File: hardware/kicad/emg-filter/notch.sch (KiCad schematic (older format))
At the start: 9 parts

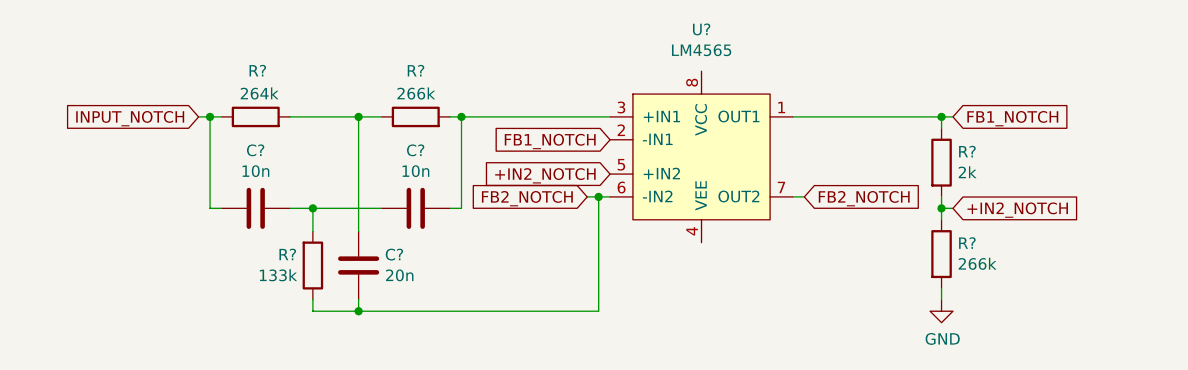
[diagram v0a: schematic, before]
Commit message: added power connections to opamp, renamed input output labels
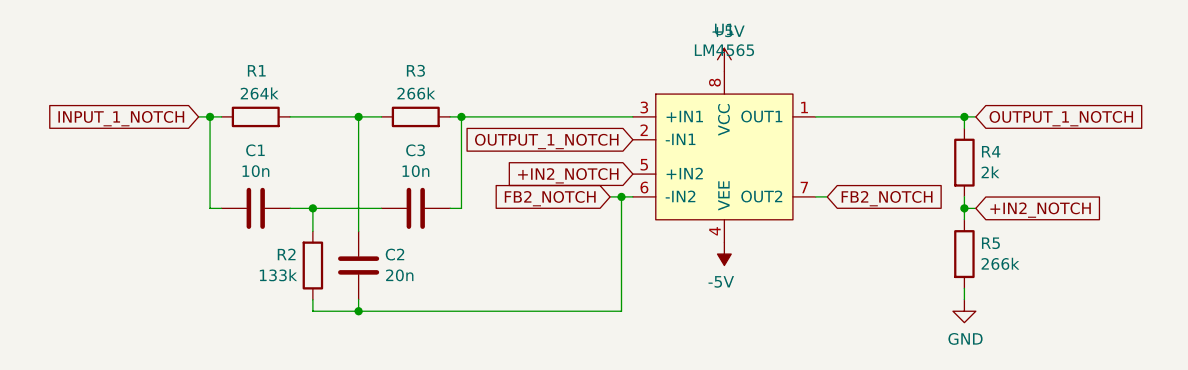
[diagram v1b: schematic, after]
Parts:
- gave numbers to parts that had none: 9
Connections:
- net -5V: now reaches U1.4 (VEE)
- net +5V: now reaches U1.8 (VCC)
- net FB1_NOTCH renamed OUTPUT_1_NOTCH
- net INPUT_NOTCH renamed INPUT_1_NOTCH
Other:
- moved on the sheet: R4, R5, U1
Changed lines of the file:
@@
 $EndDescr
 $Comp
-L emg-filter:LM4565 U?
+L emg-filter:LM4565 U1
 U 1 1 61C3A333
-P 6350 3750
-F 0 "U?" H 6350 4281 50  0000 C CNN
-F 1 "LM4565" H 6350 4190 50  0000 C CNN
-F 2 "" H 7350 3750 50  0001 C CNN
-F 3 "" H 7350 3750 50  0001 C CNN
-	1    6350 3750
-	1    0    0    -1
-$EndComp
-$Comp
-L Device:R R?
+P 6450 3750
+F 0 "U1" H 6450 4281 50  0000 C CNN
+F 1 "LM4565" H 6450 4190 50  0000 C CNN
+F 2 "" H 7450 3750 50  0001 C CNN
+F 3 "" H 7450 3750 50  0001 C CNN
+	1    6450 3750
+	1    0    0    -1
+$EndComp
+$Comp
+L Device:R R1
 U 1 1 61C3B437
 P 4400 3600
-F 0 "R?" V 4600 3550 50  0000 L CNN
+F 0 "R1" V 4600 3550 50  0000 L CNN
 F 1 "264k" V 4500 3500 50  0000 L CNN
 F 2 "" V 4330 3600 50  0001 C CNN
@@
 $EndComp
 $Comp
-L Device:R R?
+L Device:R R3
 U 1 1 61C3B5A9
 P 5100 3600
-F 0 "R?" V 5300 3600 50  0000 C CNN
+F 0 "R3" V 5300 3600 50  0000 C CNN
 F 1 "266k" V 5200 3600 50  0000 C CNN
 F 2 "" V 5030 3600 50  0001 C CNN
@@
 $EndComp
 $Comp
-L Device:R R?
+L Device:R R2
 U 1 1 61C3B840
 P 4650 4250
-F 0 "R?" H 4581 4204 50  0000 R CNN
+F 0 "R2" H 4581 4204 50  0000 R CNN
 F 1 "133k" H 4581 4295 50  0000 R CNN
 F 2 "" V 4580 4250 50  0001 C CNN
@@
 $EndComp
 $Comp
-L Device:C C?
+L Device:C C2
 U 1 1 61C3C1B8
 P 4850 4250
-F 0 "C?" H 4735 4204 50  0000 R CNN
+F 0 "C2" H 4735 4204 50  0000 R CNN
 F 1 "20n" H 4735 4295 50  0000 R CNN
 F 2 "" H 4888 4100 50  0001 C CNN
@@
 $EndComp
 $Comp
-L Device:C C?
+L Device:C C1
 U 1 1 61C3C404
 P 4400 4000
-F 0 "C?" V 4148 4000 50  0000 C CNN
+F 0 "C1" V 4148 4000 50  0000 C CNN
 F 1 "10n" V 4239 4000 50  0000 C CNN
 F 2 "" H 4438 3850 50  0001 C CNN
@@
 $EndComp
 $Comp
-L Device:C C?
+L Device:C C3
 U 1 1 61C3C5ED
 P 5100 4000
-F 0 "C?" V 4848 4000 50  0000 C CNN
+F 0 "C3" V 4848 4000 50  0000 C CNN
 F 1 "10n" V 4939 4000 50  0000 C CNN
 F 2 "" H 5138 3850 50  0001 C CNN
@@
 Wire Wire Line
 	5300 4000 5300 3600
-Text GLabel 5950 3700 0    50   Input ~ 0
-FB1_NOTCH
 Wire Wire Line
 	4650 4400 4650 4450
@@
 Wire Wire Line
 	4850 4450 4850 4400
-Text GLabel 5850 3950 0    50   Input ~ 0
+Text GLabel 5950 3950 0    50   Input ~ 0
 FB2_NOTCH
 Text GLabel 4150 3600 0    50   Input ~ 0
-INPUT_NOTCH
+INPUT_1_NOTCH
 Wire Wire Line
 	4150 3600 4200 3600
 Connection ~ 4200 3600
 Wire Wire Line
-	6750 3950 6800 3950
-Text GLabel 5950 3850 0    50   Input ~ 0
+	6850 3950 6900 3950
+Text GLabel 6050 3850 0    50   Input ~ 0
 +IN2_NOTCH
 Wire Wire Line
-	7400 4000 7400 4050
-Connection ~ 7400 4000
-Wire Wire Line
-	7400 4000 7450 4000
-Text GLabel 7450 4000 2    50   Input ~ 0
+	7500 4000 7500 4050
+Connection ~ 7500 4000
+Wire Wire Line
+	7500 4000 7550 4000
+Text GLabel 7550 4000 2    50   Input ~ 0
 +IN2_NOTCH
 Wire Wire Line
-	7400 4350 7400 4400
-$Comp
-L power:GND #PWR?
+	7500 4350 7500 4400
+$Comp
+L power:GND #PWR0104
 U 1 1 61C7C101
-P 7400 4400
-F 0 "#PWR?" H 7400 4150 50  0001 C CNN
-F 1 "GND" H 7405 4227 50  0000 C CNN
-F 2 "" H 7400 4400 50  0001 C CNN
-F 3 "" H 7400 4400 50  0001 C CNN
-	1    7400 4400
-	1    0    0    -1
-$EndComp
-Connection ~ 7400 3600
-Wire Wire Line
-	6750 3600 7400 3600
-Wire Wire Line
-	7400 3600 7450 3600
-Wire Wire Line
-	7400 3600 7400 3650
-Wire Wire Line
-	7400 3950 7400 4000
-Text GLabel 6800 3950 2    50   Input ~ 0
+P 7500 4400
+F 0 "#PWR0104" H 7500 4150 50  0001 C CNN
+F 1 "GND" H 7505 4227 50  0000 C CNN
+F 2 "" H 7500 4400 50  0001 C CNN
+F 3 "" H 7500 4400 50  0001 C CNN
+	1    7500 4400
+	1    0    0    -1
+$EndComp
+Connection ~ 7500 3600
+Wire Wire Line
+	6850 3600 7500 3600
+Wire Wire Line
+	7500 3600 7550 3600
+Wire Wire Line
+	7500 3600 7500 3650
+Wire Wire Line
+	7500 3950 7500 4000
+Text GLabel 6900 3950 2    50   Input ~ 0
 FB2_NOTCH
-Text GLabel 7450 3600 2    50   Input ~ 0
-FB1_NOTCH
-$Comp
-L Device:R R?
+Text GLabel 7550 3600 2    50   Input ~ 0
+OUTPUT_1_NOTCH
+$Comp
+L Device:R R4
 U 1 1 61C3BC8C
-P 7400 3800
-F 0 "R?" H 7470 3846 50  0000 L CNN
-F 1 "2k" H 7470 3755 50  0000 L CNN
-F 2 "" V 7330 3800 50  0001 C CNN
-F 3 "~" H 7400 3800 50  0001 C CNN
-	1    7400 3800
-	1    0    0    -1
-$EndComp
-$Comp
-L Device:R R?
+P 7500 3800
+F 0 "R4" H 7570 3846 50  0000 L CNN
+F 1 "2k" H 7570 3755 50  0000 L CNN
+F 2 "" V 7430 3800 50  0001 C CNN
+F 3 "~" H 7500 3800 50  0001 C CNN
+	1    7500 3800
+	1    0    0    -1
+$EndComp
+$Comp
+L Device:R R5
 U 1 1 61C3BADF
-P 7400 4200
-F 0 "R?" H 7470 4246 50  0000 L CNN
-F 1 "266k" H 7470 4155 50  0000 L CNN
-F 2 "" V 7330 4200 50  0001 C CNN
-F 3 "~" H 7400 4200 50  0001 C CNN
-	1    7400 4200
-	1    0    0    -1
-$EndComp
-Wire Wire Line
-	5850 3950 5900 3950
-Wire Wire Line
-	5300 3600 5950 3600
+P 7500 4200
+F 0 "R5" H 7570 4246 50  0000 L CNN
+F 1 "266k" H 7570 4155 50  0000 L CNN
+F 2 "" V 7430 4200 50  0001 C CNN
+F 3 "~" H 7500 4200 50  0001 C CNN
+	1    7500 4200
+	1    0    0    -1
+$EndComp
+Wire Wire Line
+	5950 3950 6000 3950
+Wire Wire Line
+	5300 3600 6050 3600
+Wire Wire Line
+	4850 4450 6000 4450
+Wire Wire Line
+	6000 4450 6000 3950
+Connection ~ 6000 3950
+Wire Wire Line
+	6000 3950 6050 3950
+$Comp
+L power:+5V #PWR0105
+U 1 1 61C3E5E0
+P 6450 3400
+F 0 "#PWR0105" H 6450 3250 50  0001 C CNN
+F 1 "+5V" H 6465 3573 50  0000 C CNN
+F 2 "" H 6450 3400 50  0001 C CNN
+F 3 "" H 6450 3400 50  0001 C CNN
+	1    6450 3400
+	1    0    0    -1
+$EndComp
+$Comp
+L power:-5V #PWR0106
+U 1 1 61C3F0F8
+P 6450 4150
+F 0 "#PWR0106" H 6450 4250 50  0001 C CNN
+F 1 "-5V" H 6465 4323 50  0000 C CNN
+F 2 "" H 6450 4150 50  0001 C CNN
+F 3 "" H 6450 4150 50  0001 C CNN
+	1    6450 4150
+	-1   0    0    1
+$EndComp
+Text GLabel 6050 3700 0    50   Input ~ 0
+OUTPUT_1_NOTCH
 Connection ~ 5300 3600
-Wire Wire Line
-	4850 4450 5900 4450
-Wire Wire Line
-	5900 4450 5900 3950
 Connection ~ 4850 4450
-Connection ~ 5900 3950
-Wire Wire Line
-	5900 3950 5950 3950
 $EndSCHEMATC

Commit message: notch x16
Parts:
- added C? (x7): 20n, symbol Device:C
- added C? (x14): 10n, symbol Device:C
- added R? (x14): 266k, symbol Device:R
- added R? (x7): 133k, symbol Device:R
- added R? (x7): 2k, symbol Device:R
- added R? (x7): 264k, symbol Device:R
- added U? (x7): LM4565, symbol emg-filter:LM4565
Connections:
- net +5V: now also U?.8 (VCC), U?.8 (VCC), U?.8 (VCC), U?.8 (VCC), U?.8 (VCC), U?.8 (VCC), U?.8 (VCC)
- net -5V: now also U?.4 (VEE), U?.4 (VEE), U?.4 (VEE), U?.4 (VEE), U?.4 (VEE), U?.4 (VEE), U?.4 (VEE)
- net GND: now also R?.2, R?.2, R?.2, R?.2, R?.2, R?.2, R?.2
- net +IN2_NOTCH renamed +IN2_1_NOTCH
- net FB2_NOTCH: no longer names the net of C2.1, R2.1, U1.6 (-IN2), U1.7 (OUT2)
- new net: C?.1, R?.2, U?.3 (+IN1) (x7)
- new net: C?.1, R?.1, U?.6 (-IN2), U?.7 (OUT2) (x7)
- new net: C?.2, R?.1, R?.2 (x7)
- new net: C?.1, C?.2, R?.2 (x7)
- new net +IN2_2_NOTCH: R?.1, R?.2, U?.5 (+IN2)
- new net +IN2_3_NOTCH: R?.1, R?.2, U?.5 (+IN2)
- new net +IN2_4_NOTCH: R?.1, R?.2, U?.5 (+IN2)
- new net +IN2_5_NOTCH: R?.1, R?.2, U?.5 (+IN2)
- new net +IN2_6_NOTCH: R?.1, R?.2, U?.5 (+IN2)
- new net +IN2_7_NOTCH: R?.1, R?.2, U?.5 (+IN2)
- new net +IN2_8_NOTCH: R?.1, R?.2, U?.5 (+IN2)
- new net INPUT_2_NOTCH: C?.2, R?.1
- new net INPUT_3_NOTCH: C?.2, R?.1
- new net INPUT_4_NOTCH: C?.2, R?.1
- new net INPUT_5_NOTCH: C?.2, R?.1
- new net INPUT_6_NOTCH: C?.2, R?.1
- new net INPUT_7_NOTCH: C?.2, R?.1
- new net INPUT_8_NOTCH: C?.2, R?.1
- new net OUTPUT_2_NOTCH: R?.1, U?.1 (OUT1), U?.2 (-IN1)
- new net OUTPUT_3_NOTCH: R?.1, U?.1 (OUT1), U?.2 (-IN1)
- new net OUTPUT_4_NOTCH: R?.1, U?.1 (OUT1), U?.2 (-IN1)
- new net OUTPUT_5_NOTCH: R?.1, U?.1 (OUT1), U?.2 (-IN1)
- new net OUTPUT_6_NOTCH: R?.1, U?.1 (OUT1), U?.2 (-IN1)
- new net OUTPUT_7_NOTCH: R?.1, U?.1 (OUT1), U?.2 (-IN1)
- new net OUTPUT_8_NOTCH: R?.1, U?.1 (OUT1), U?.2 (-IN1)
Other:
- moved on the sheet: C1, C2, C3, R1, R2, R3, R4, R5, U1

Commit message: annotation
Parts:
- gave numbers to parts that had none: 63
- renumbered C1 to C52, C2 to C56, C3 to C60, R1 to R76, R2 to R80, R3 to R84, R4 to R89, R5 to R90, U1 to U21

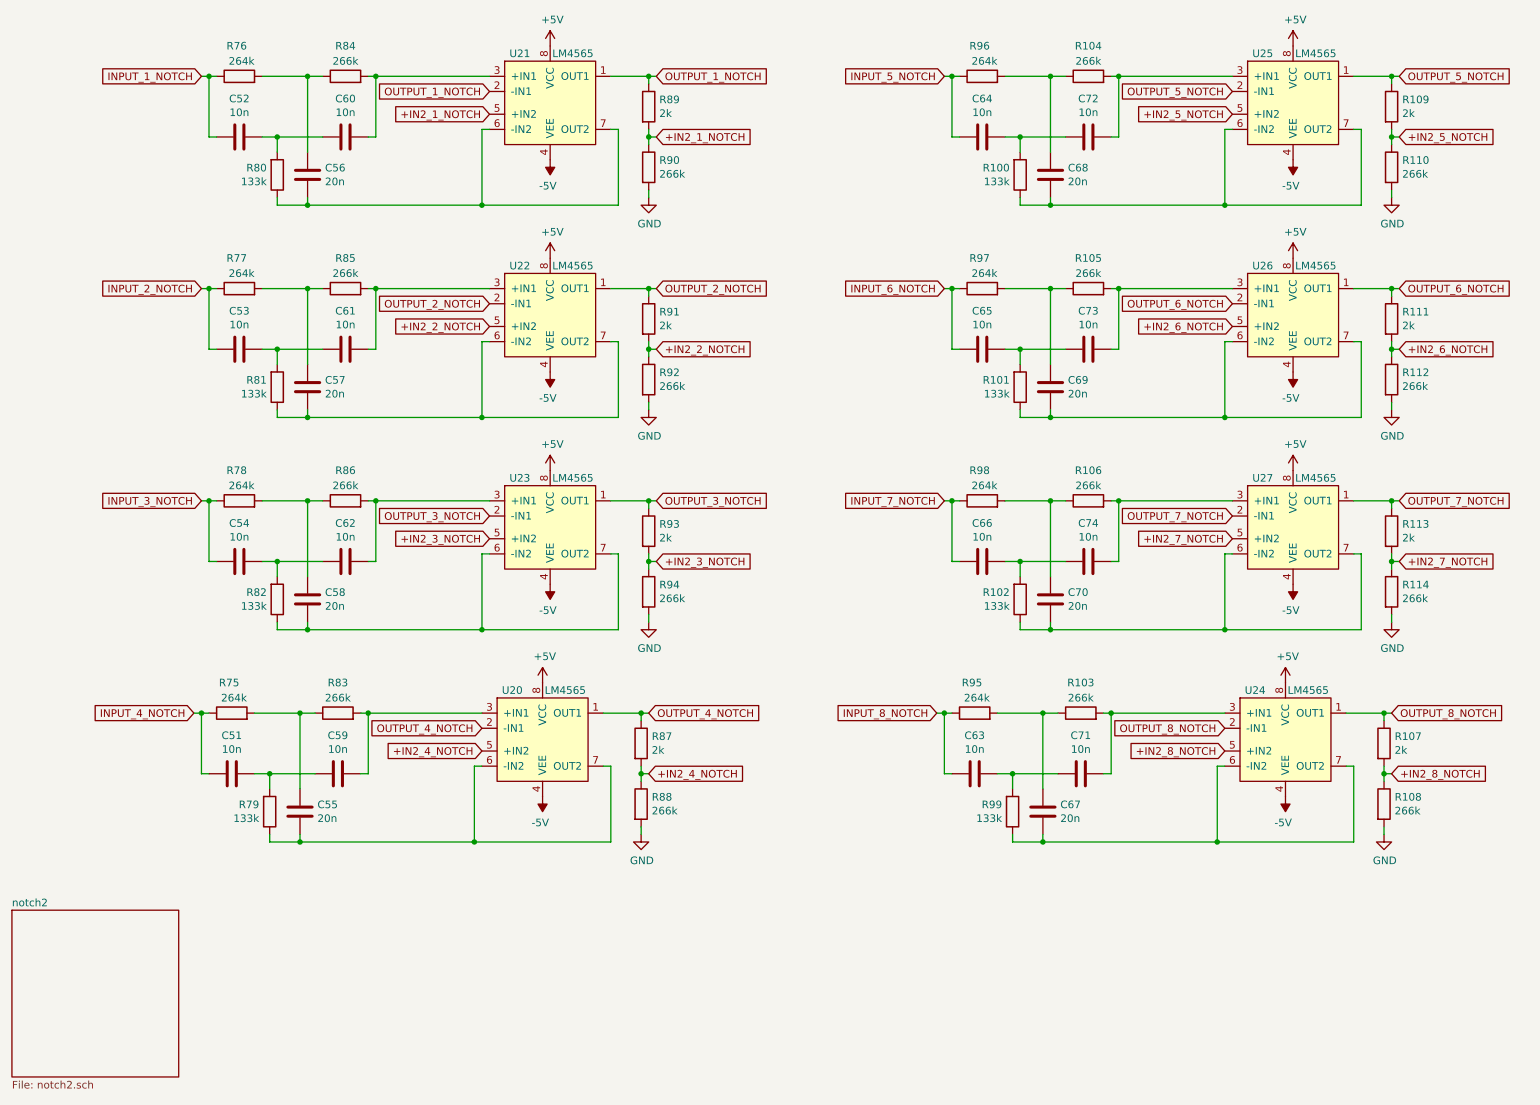
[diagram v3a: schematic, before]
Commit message: linked stages by renaming labels
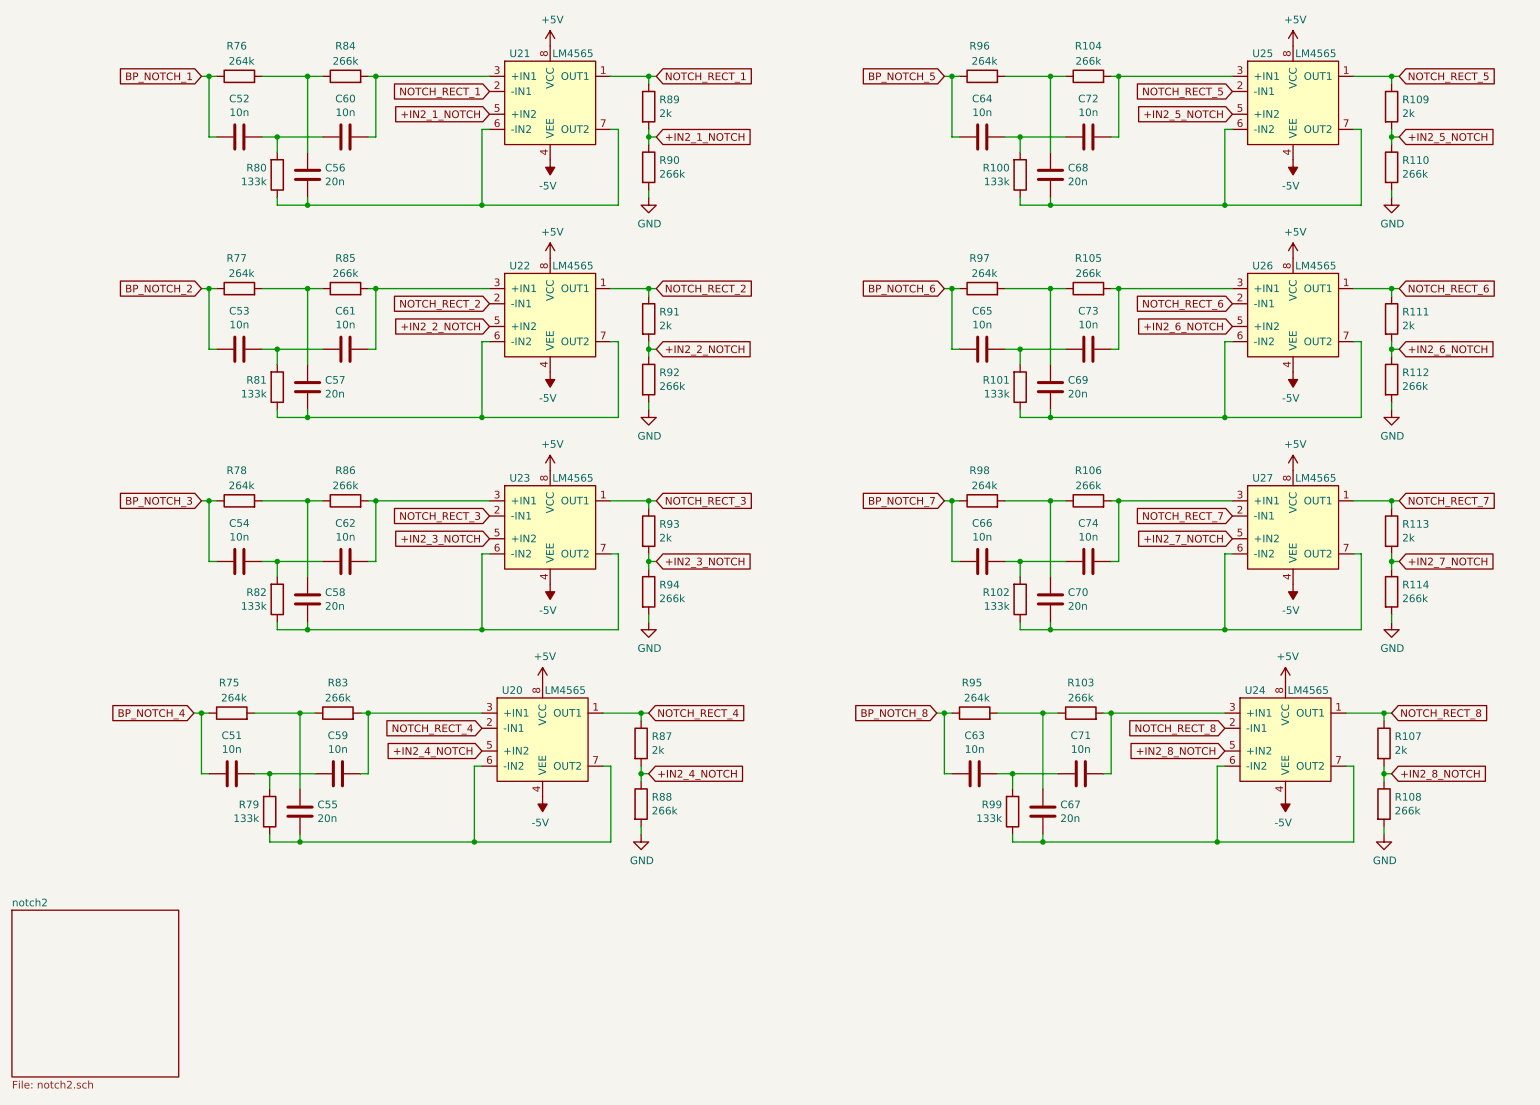
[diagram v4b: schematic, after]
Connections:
- net INPUT_1_NOTCH renamed BP_NOTCH_1
- net INPUT_2_NOTCH renamed BP_NOTCH_2
- net INPUT_3_NOTCH renamed BP_NOTCH_3
- net INPUT_4_NOTCH renamed BP_NOTCH_4
- net INPUT_5_NOTCH renamed BP_NOTCH_5
- net INPUT_6_NOTCH renamed BP_NOTCH_6
- net INPUT_7_NOTCH renamed BP_NOTCH_7
- net INPUT_8_NOTCH renamed BP_NOTCH_8
- net OUTPUT_1_NOTCH renamed NOTCH_RECT_1
- net OUTPUT_2_NOTCH renamed NOTCH_RECT_2
- net OUTPUT_3_NOTCH renamed NOTCH_RECT_3
- net OUTPUT_4_NOTCH renamed NOTCH_RECT_4
- net OUTPUT_5_NOTCH renamed NOTCH_RECT_5
- net OUTPUT_6_NOTCH renamed NOTCH_RECT_6
- net OUTPUT_7_NOTCH renamed NOTCH_RECT_7
- net OUTPUT_8_NOTCH renamed NOTCH_RECT_8
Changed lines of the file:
@@
 Wire Wire Line
 	2600 1850 2600 1800
-Text GLabel 1900 1000 0    50   Input ~ 0
-INPUT_1_NOTCH
 Wire Wire Line
 	1900 1000 1950 1000
@@
 Wire Wire Line
 	4850 1350 4850 1400
-Text GLabel 4900 1000 2    50   Input ~ 0
-OUTPUT_1_NOTCH
 $Comp
 L Device:R R89
@@
 	-1   0    0    1
 $EndComp
-Text GLabel 3800 1100 0    50   Input ~ 0
-OUTPUT_1_NOTCH
 Connection ~ 3050 1000
 Connection ~ 2600 1850
@@
 Wire Wire Line
 	2600 3250 2600 3200
-Text GLabel 1900 2400 0    50   Input ~ 0
-INPUT_2_NOTCH
 Wire Wire Line
 	1900 2400 1950 2400
@@
 Wire Wire Line
 	4850 2750 4850 2800
-Text GLabel 4900 2400 2    50   Input ~ 0
-OUTPUT_2_NOTCH
 $Comp
 L Device:R R91
@@
 	-1   0    0    1
 $EndComp
-Text GLabel 3800 2500 0    50   Input ~ 0
-OUTPUT_2_NOTCH
 Connection ~ 3050 2400
 Connection ~ 2600 3250
@@
 Wire Wire Line
 	2600 4650 2600 4600
-Text GLabel 1900 3800 0    50   Input ~ 0
-INPUT_3_NOTCH
 Wire Wire Line
 	1900 3800 1950 3800
@@
 Wire Wire Line
 	4850 4150 4850 4200
-Text GLabel 4900 3800 2    50   Input ~ 0
-OUTPUT_3_NOTCH
 $Comp
 L Device:R R93
@@
 	-1   0    0    1
 $EndComp
-Text GLabel 3800 3900 0    50   Input ~ 0
-OUTPUT_3_NOTCH
 Connection ~ 3050 3800
 Connection ~ 2600 4650
@@
 Wire Wire Line
 	2550 6050 2550 6000
-Text GLabel 1850 5200 0    50   Input ~ 0
-INPUT_4_NOTCH
 Wire Wire Line
 	1850 5200 1900 5200
@@
 Wire Wire Line
 	4800 5550 4800 5600
-Text GLabel 4850 5200 2    50   Input ~ 0
-OUTPUT_4_NOTCH
 $Comp
 L Device:R R87
@@
 	-1   0    0    1
 $EndComp
-Text GLabel 3750 5300 0    50   Input ~ 0
-OUTPUT_4_NOTCH
 Connection ~ 3000 5200
 Connection ~ 2550 6050
@@
 Wire Wire Line
 	7500 1850 7500 1800
-Text GLabel 6800 1000 0    50   Input ~ 0
-INPUT_5_NOTCH
 Wire Wire Line
 	6800 1000 6850 1000
@@
 Wire Wire Line
 	9750 1350 9750 1400
-Text GLabel 9800 1000 2    50   Input ~ 0
-OUTPUT_5_NOTCH
 $Comp
 L Device:R R109
@@
 	-1   0    0    1
 $EndComp
-Text GLabel 8700 1100 0    50   Input ~ 0
-OUTPUT_5_NOTCH
 Connection ~ 7950 1000
 Connection ~ 7500 1850
@@
 Wire Wire Line
 	7500 3250 7500 3200
-Text GLabel 6800 2400 0    50   Input ~ 0
-INPUT_6_NOTCH
 Wire Wire Line
 	6800 2400 6850 2400
@@
 Wire Wire Line
 	9750 2750 9750 2800
-Text GLabel 9800 2400 2    50   Input ~ 0
-OUTPUT_6_NOTCH
 $Comp
 L Device:R R111
@@
 	-1   0    0    1
 $EndComp
-Text GLabel 8700 2500 0    50   Input ~ 0
-OUTPUT_6_NOTCH
 Connection ~ 7950 2400
 Connection ~ 7500 3250
@@
 Wire Wire Line
 	7500 4650 7500 4600
-Text GLabel 6800 3800 0    50   Input ~ 0
-INPUT_7_NOTCH
 Wire Wire Line
 	6800 3800 6850 3800
@@
 Wire Wire Line
 	9750 4150 9750 4200
-Text GLabel 9800 3800 2    50   Input ~ 0
-OUTPUT_7_NOTCH
 $Comp
 L Device:R R113
@@
 	-1   0    0    1
 $EndComp
-Text GLabel 8700 3900 0    50   Input ~ 0
-OUTPUT_7_NOTCH
 Connection ~ 7950 3800
 Connection ~ 7500 4650
@@
 F1 "notch2.sch" 50
 $EndSheet
-Text GLabel 6750 5200 0    50   Input ~ 0
-INPUT_8_NOTCH
-Text GLabel 8650 5300 0    50   Input ~ 0
-OUTPUT_8_NOTCH
 Text GLabel 8650 5450 0    50   Input ~ 0
 +IN2_8_NOTCH
-Text GLabel 9750 5200 2    50   Input ~ 0
-OUTPUT_8_NOTCH
 Text GLabel 9750 5600 2    50   Input ~ 0
 +IN2_8_NOTCH
+Text GLabel 1900 1000 0    50   Input ~ 0
+BP_NOTCH_1
+Text GLabel 1900 2400 0    50   Input ~ 0
+BP_NOTCH_2
+Text GLabel 1900 3800 0    50   Input ~ 0
+BP_NOTCH_3
+Text GLabel 1850 5200 0    50   Input ~ 0
+BP_NOTCH_4
+Text GLabel 6800 1000 0    50   Input ~ 0
+BP_NOTCH_5
+Text GLabel 6800 2400 0    50   Input ~ 0
+BP_NOTCH_6
+Text GLabel 6800 3800 0    50   Input ~ 0
+BP_NOTCH_7
+Text GLabel 6750 5200 0    50   Input ~ 0
+BP_NOTCH_8
+Text GLabel 4900 1000 2    50   Input ~ 0
+NOTCH_RECT_1
+Text GLabel 4900 2400 2    50   Input ~ 0
+NOTCH_RECT_2
+Text GLabel 4900 3800 2    50   Input ~ 0
+NOTCH_RECT_3
+Text GLabel 4850 5200 2    50   Input ~ 0
+NOTCH_RECT_4
+Text GLabel 9800 1000 2    50   Input ~ 0
+NOTCH_RECT_5
+Text GLabel 9800 2400 2    50   Input ~ 0
+NOTCH_RECT_6
+Text GLabel 9800 3800 2    50   Input ~ 0
+NOTCH_RECT_7
+Text GLabel 9750 5200 2    50   Input ~ 0
+NOTCH_RECT_8
+Text GLabel 3800 1100 0    50   Input ~ 0
+NOTCH_RECT_1
+Text GLabel 3800 2500 0    50   Input ~ 0
+NOTCH_RECT_2
+Text GLabel 3800 3900 0    50   Input ~ 0
+NOTCH_RECT_3
+Text GLabel 3750 5300 0    50   Input ~ 0
+NOTCH_RECT_4
+Text GLabel 8700 1100 0    50   Input ~ 0
+NOTCH_RECT_5
+Text GLabel 8700 2500 0    50   Input ~ 0
+NOTCH_RECT_6
+Text GLabel 8700 3900 0    50   Input ~ 0
+NOTCH_RECT_7
+Text GLabel 8650 5300 0    50   Input ~ 0
+NOTCH_RECT_8
 $EndSCHEMATC
